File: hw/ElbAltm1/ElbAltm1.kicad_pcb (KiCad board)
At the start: 2 copper layers, 40.6 x 45.7 mm, 38 parts, among them J1 USB_C_Receptacle, J2 SWD, Q1 BC818, SW1 BUTT1, SW2 BUTT1, SW3 BUTT1, U1 MCP1703Ax-330xxTT, U2 OLED 128x64, U3 STM32C071FBPx, U4 MS5611-01BA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

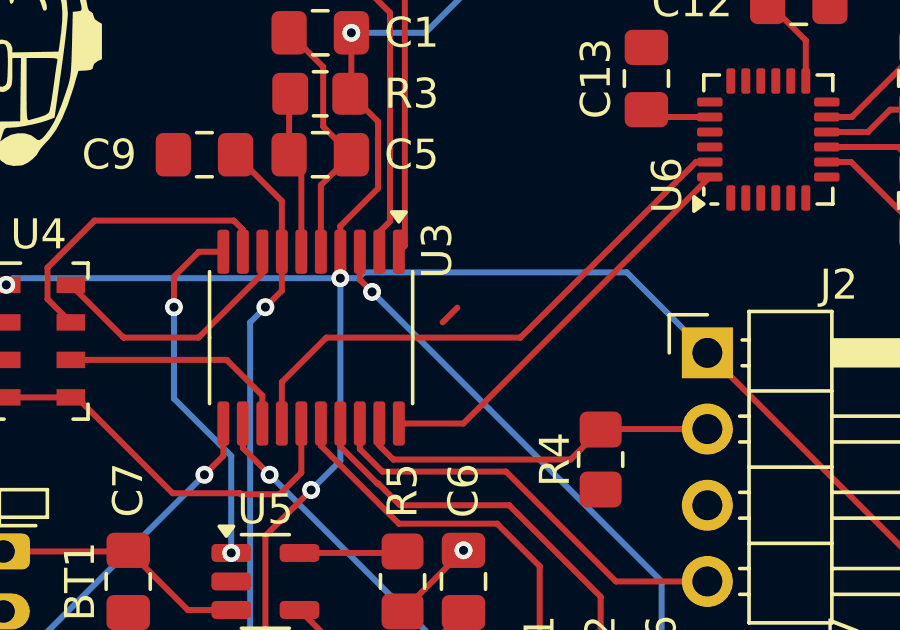
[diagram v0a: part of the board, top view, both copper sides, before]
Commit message: Ritardo prima della inizializzazione OLED
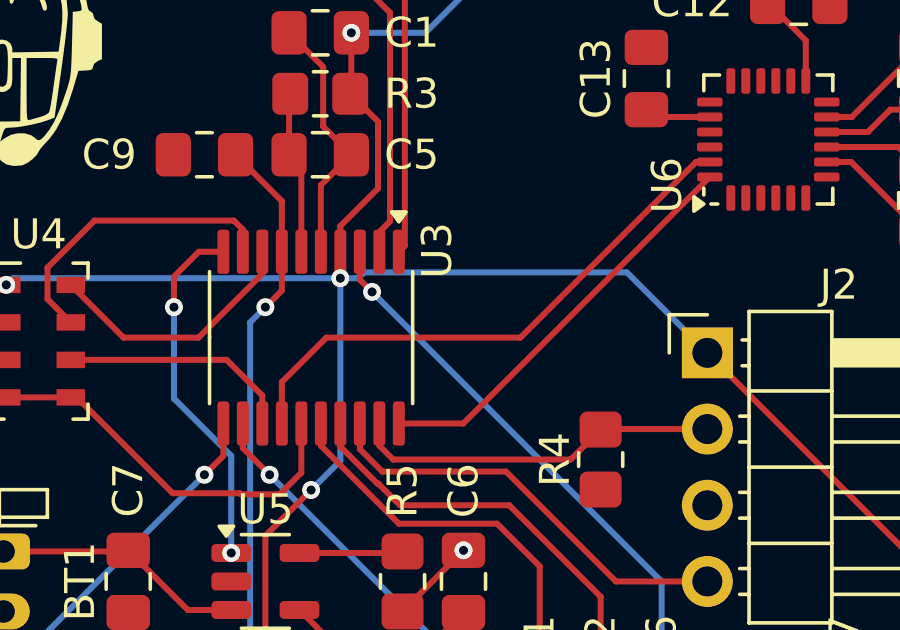
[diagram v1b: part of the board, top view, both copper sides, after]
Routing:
- net GND: track 19.7 -> 19.0 mm
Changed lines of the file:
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@@
-	)
-	(segment
-		(start 150.688 92.964)
-		(end 151.18 92.472)
-		(width 0.2)
-		(layer "F.Cu")
-		(net 2)
 	)
 	(segment
